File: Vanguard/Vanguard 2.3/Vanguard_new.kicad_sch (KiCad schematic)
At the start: 84 parts, among them J1 USB_C_Receptacle_USB2.0_16P, J2 Conn_02x03_Pin, J3 Micro_SD_Card_Det1, J4 STARBOARD_SERVO, J5 PORTSIDE_SERVO, J6 Conn_01x02_Pin, J7 EJECTION_SERVO, Q1 BSS138, Q2 BSS138, Q3 BSS138, Q4 BSS138, U1 ATSAMD11D14A-M, U2 ATmega4809-A, U3 AT25DF641A-SH-T, U4 AP2112K-3.3, U5 BD1020HFV, U6 BNO086, U7 TXB0104D, U8 TPS61092, U9 MPM3610AGQV-P, Y1 32.768kHz

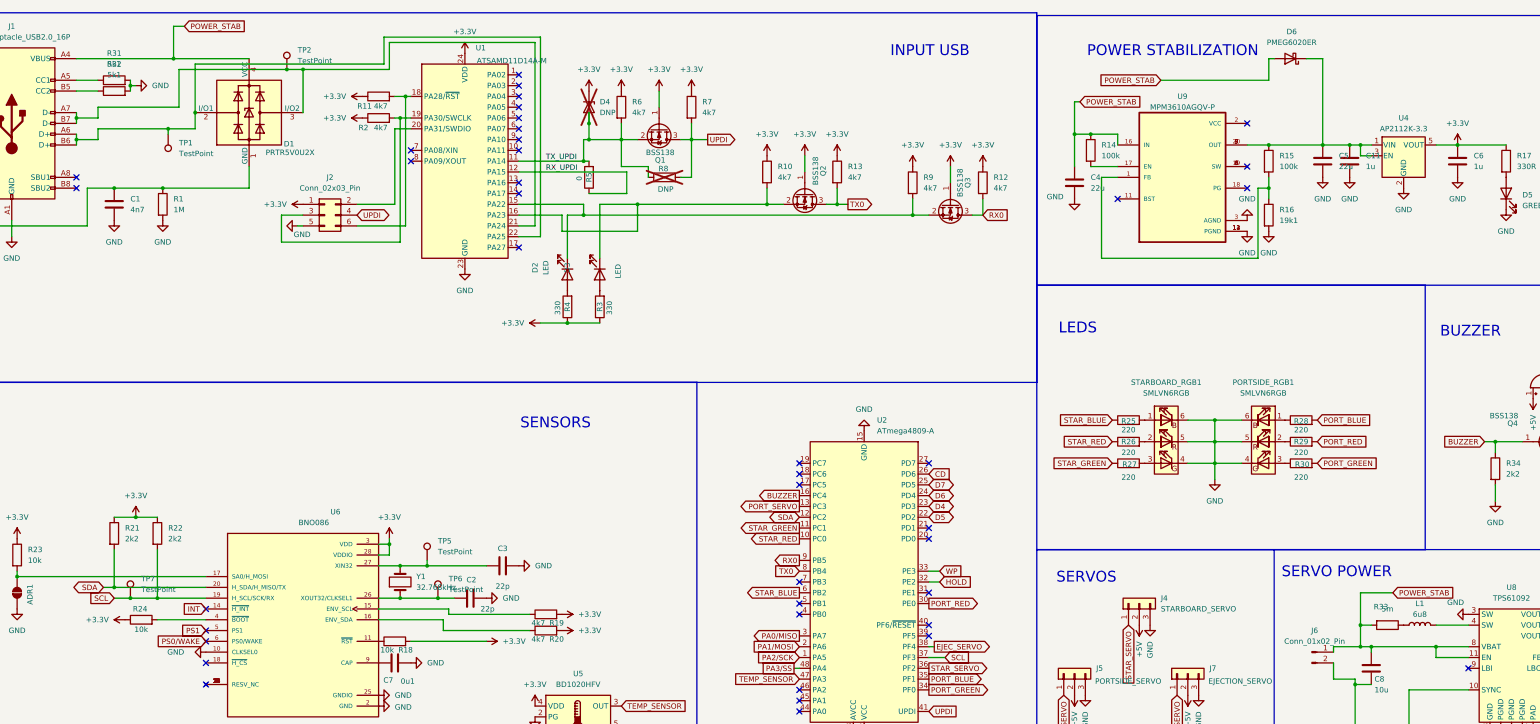
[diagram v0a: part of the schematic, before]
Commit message: diode added on vbus of usb c
prevents back driving device on usbc line. Led added for power on indication.
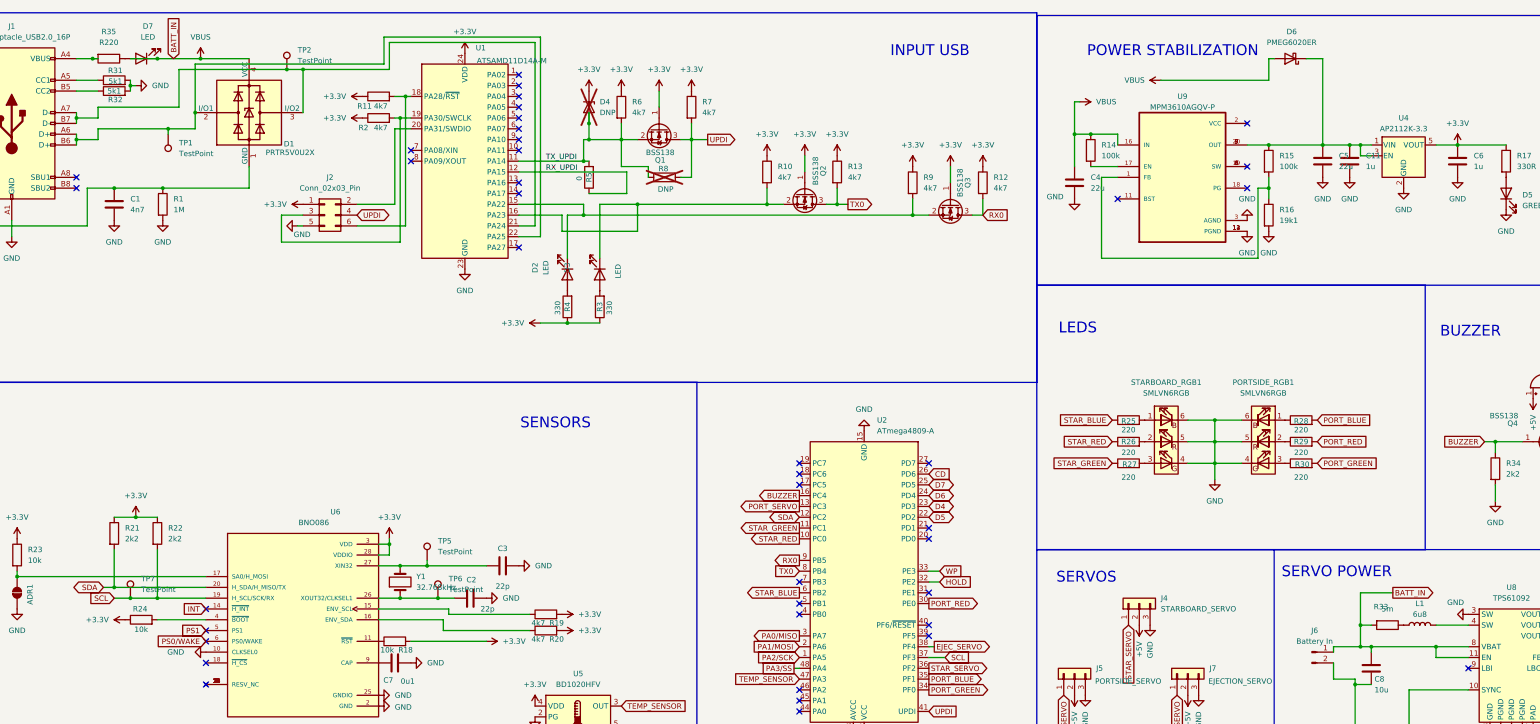
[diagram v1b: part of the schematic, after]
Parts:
- added D7: LED, LED_SMD:LED_0201_0603Metric, symbol Device:LED
- added R35: R220, Resistor_SMD:R_0402_1005Metric, symbol Device:R
- J6: value Conn_01x02_Pin -> Battery In
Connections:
- net POWER_STAB renamed VBUS
- net VBUS: now also D7.1 (K); no longer J1.A4 (VBUS), J1.A9 (VBUS), J1.B4 (VBUS), J1.B9 (VBUS)
- new net: D7.2 (A), R35.1
- new net: J1.A4 (VBUS), J1.A9 (VBUS), J1.B4 (VBUS), J1.B9 (VBUS), R35.2
